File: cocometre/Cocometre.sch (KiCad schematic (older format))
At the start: 20 parts, among them P1 CONN_01X05, P2 CONN_01X05, U2 LTC4316

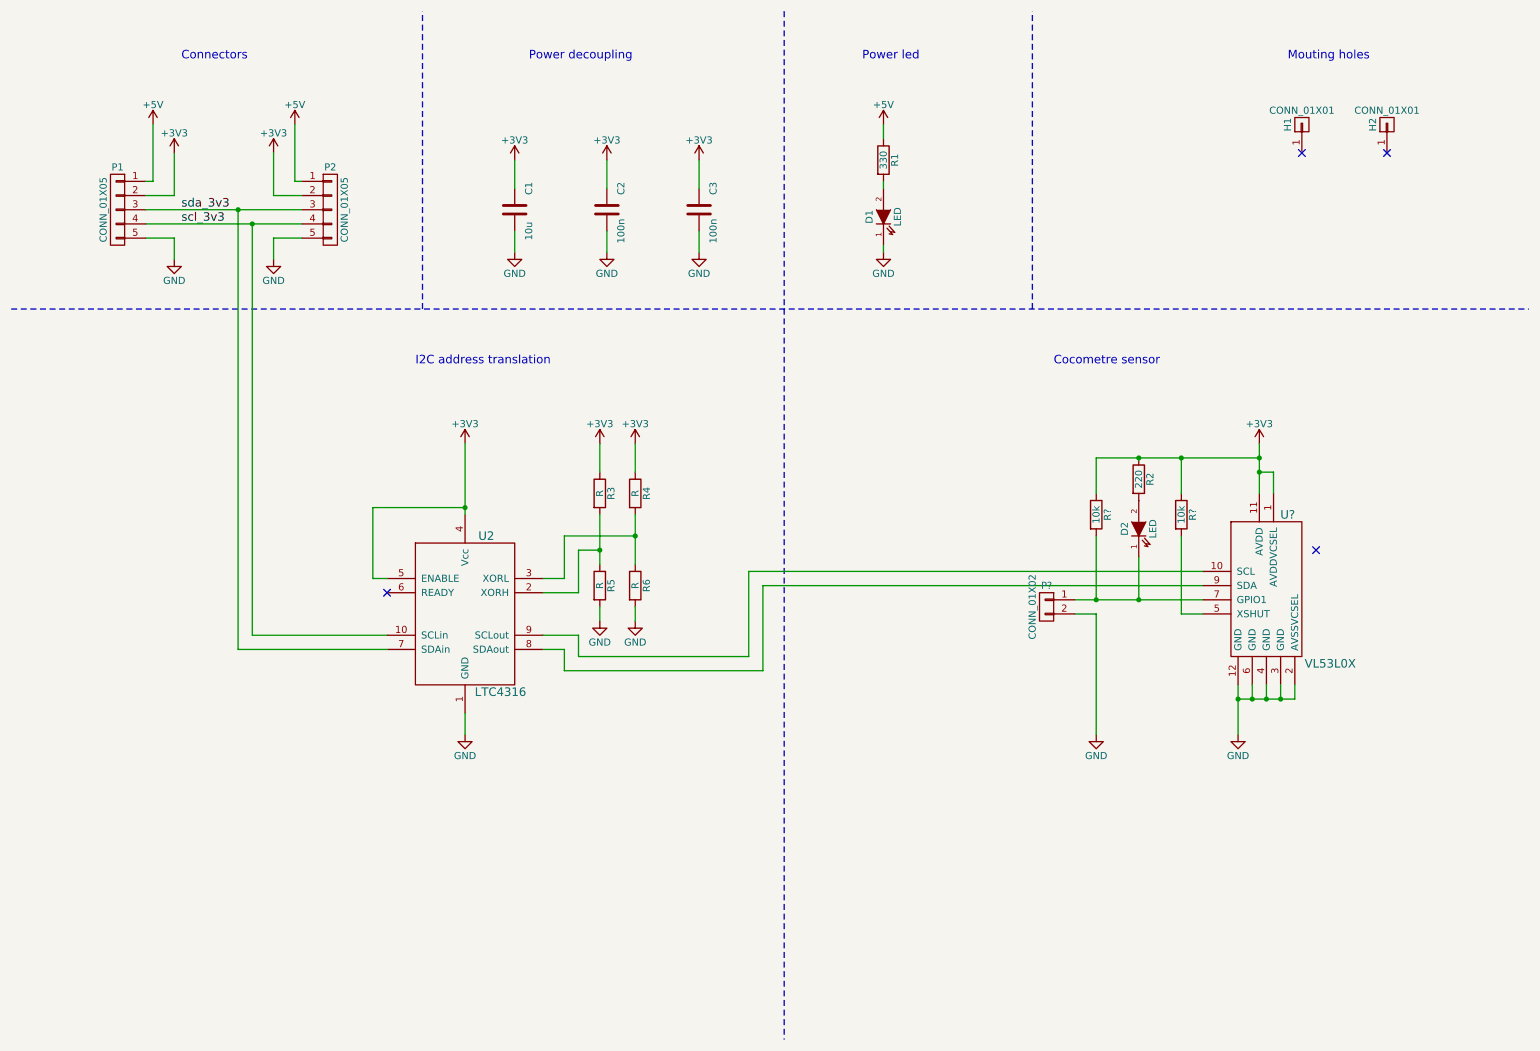
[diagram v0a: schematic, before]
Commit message: Cocometre layout
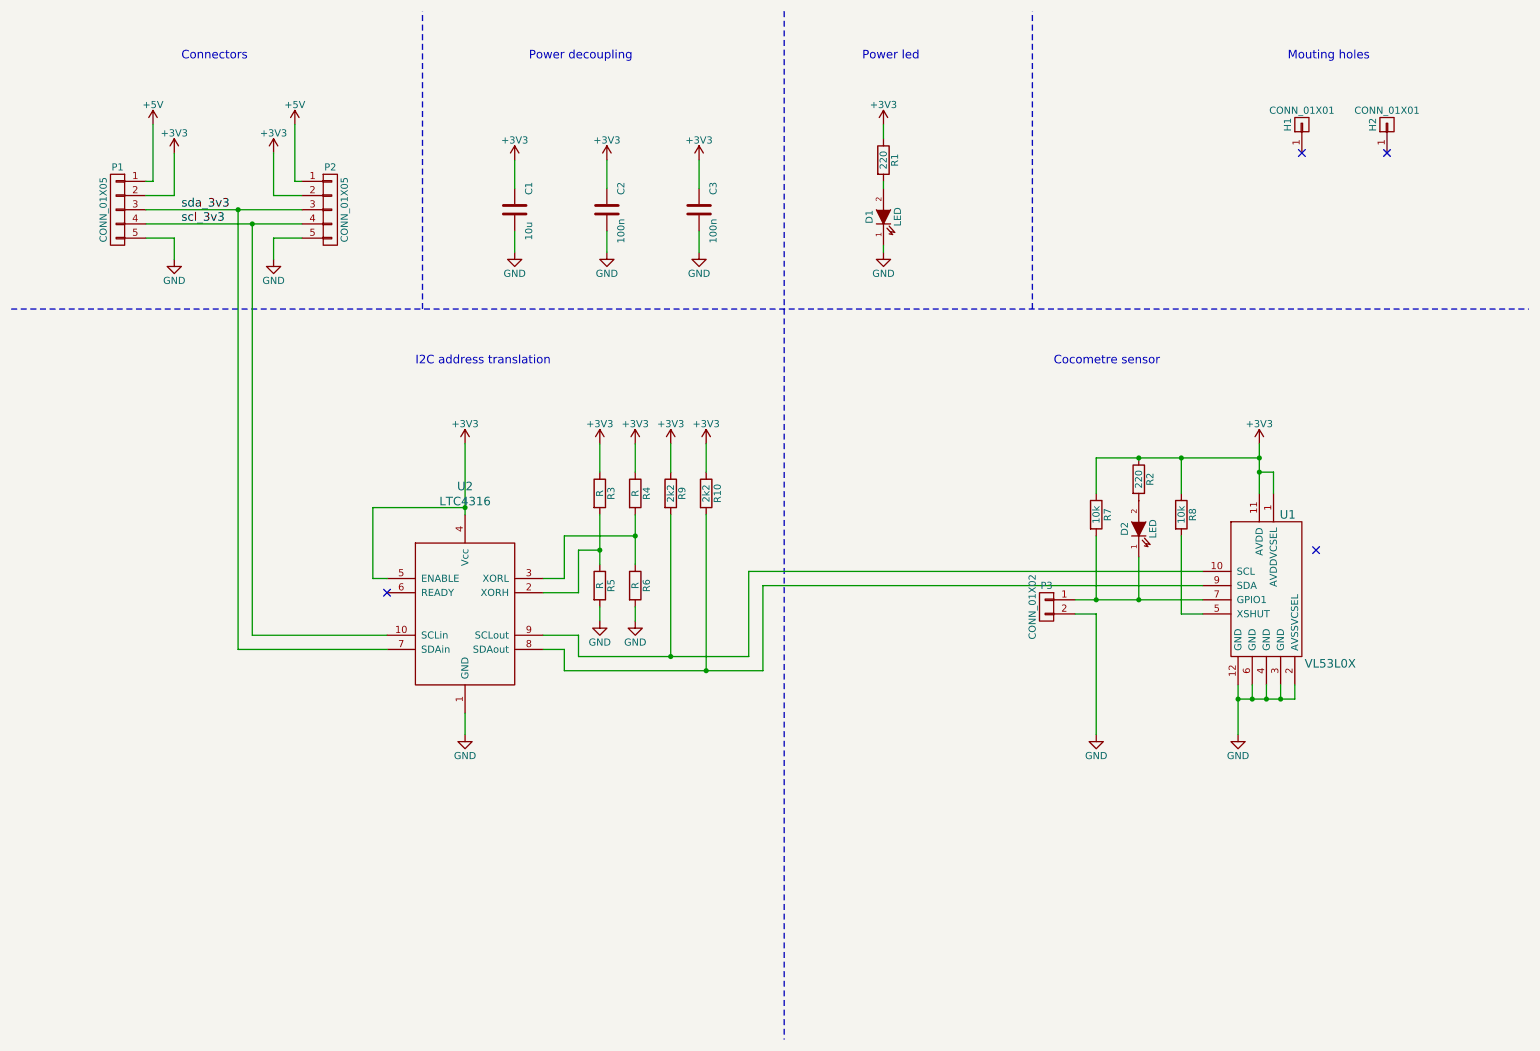
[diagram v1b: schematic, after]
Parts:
- added R10, R9: 2k2, espitall:R_0603_HandSoldering, symbol R
- C1: footprint (none) -> espitall:C_0805_HandSoldering
- C2, C3: footprint (none) -> espitall:C_0603_HandSoldering
- D1, D2: footprint (none) -> espitall:LED_0805
- H1, H2: footprint (none) -> Mounting_Holes:MountingHole_3.2mm_M3
- P1, P2: footprint (none) -> espitall:Socket_MOLEX-KK-RM2-54mm_Lock_5pin_straight
- P3: renamed from P?; footprint (none) -> espitall:Socket_MOLEX-KK-RM2-54mm_Lock_2pin_straight
- R1: value 330 -> 220; footprint (none) -> espitall:R_0603_HandSoldering
- R2, R3, R4, R5, R6: footprint (none) -> espitall:R_0603_HandSoldering
- R7, R8: renamed from R?; footprint (none) -> espitall:R_0603_HandSoldering
- U1: renamed from U?; footprint (none) -> espitall:VL53L0X
- U2: footprint (none) -> espitall:MSOP-10
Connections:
- net +3V3: now also R1.1, R10.1, R9.1
- net +5V: no longer R1.1
- net at U1.9 (SDA), U2.8 (SDAout): now also R10.2
- net at U1.10 (SCL), U2.9 (SCLout): now also R9.2
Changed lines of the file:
@@
-EESchema Schematic File Version 2
-LIBS:xilinx
-LIBS:video
-LIBS:valves
-LIBS:ttl_ieee
-LIBS:transistors
-LIBS:transf
-LIBS:texas
-LIBS:switches
-LIBS:supertex
-LIBS:stm8
-LIBS:stm32
-LIBS:siliconi
-LIBS:silabs
-LIBS:sensors
-LIBS:rfcom
-LIBS:relays
-LIBS:regul
-LIBS:references
-LIBS:powerint
-LIBS:power
-LIBS:philips
-LIBS:opto
-LIBS:onsemi
-LIBS:nxp_armmcu
-LIBS:nordicsemi
-LIBS:msp430
-LIBS:motorola
-LIBS:motor_drivers
-LIBS:microcontrollers
-LIBS:microchip_pic32mcu
-LIBS:microchip_pic18mcu
-LIBS:microchip_pic16mcu
-LIBS:microchip_pic12mcu
-LIBS:microchip_pic10mcu
-LIBS:microchip_dspic33dsc
-LIBS:microchip
-LIBS:memory
-LIBS:maxim
-LIBS:logo
-LIBS:linear
-LIBS:ir
-LIBS:interface
-LIBS:intel
-LIBS:hc11
-LIBS:graphic
-LIBS:gennum
-LIBS:ftdi
-LIBS:elec-unifil
-LIBS:dsp
-LIBS:display
-LIBS:diode
-LIBS:digital-audio
-LIBS:device
-LIBS:dc-dc
-LIBS:cypress
-LIBS:contrib
-LIBS:conn
-LIBS:cmos_ieee
-LIBS:cmos4000
-LIBS:brooktre
-LIBS:audio
-LIBS:atmel
-LIBS:analog_switches
-LIBS:analog_devices
-LIBS:adc-dac
-LIBS:actel
-LIBS:ac-dc
-LIBS:Zilog
-LIBS:Xicor
-LIBS:Power_Management
-LIBS:Oscillators
-LIBS:Lattice
-LIBS:ESD_Protection
-LIBS:Altera
-LIBS:74xx
-LIBS:74xgxx
-LIBS:Symbols_Transformer-Diskrete_RevA
-LIBS:Symbols_Socket-DIN41612_RevA
-LIBS:Symbols_Microcontroller_Philips-NXP_RevA_06Oct2013
-LIBS:Symbols_ICs-Opto_RevB_16Sep2013
-LIBS:Symbols_ICs-Diskrete_RevD10
-LIBS:Symbols_EN60617_13Mar2013
-LIBS:Symbols_EN60617-10_HF-Radio_DRAFT_12Sep2013
-LIBS:Symbols_DCDC-ACDC-Converter_RevC_20Jul2012
-LIBS:SymbolsSimilarEN60617+oldDIN617-RevE8
+EESchema Schematic File Version 3
 LIBS:espitall
 LIBS:Cocometre-cache
-EELAYER 25 0
+EELAYER 26 0
 EELAYER END
 $Descr A4 11693 8268
@@
 $EndComp
 $Comp
-L LTC4316 U2
-U 1 1 573CCB68
-P 3700 4750
-F 0 "U2" H 3850 5300 60  0000 C CNN
-F 1 "LTC4316" H 3950 4200 60  0000 C CNN
-F 2 "" H 3700 4750 60  0000 C CNN
-F 3 "" H 3700 4750 60  0000 C CNN
-	1    3700 4750
-	1    0    0    -1
-$EndComp
-$Comp
 L R R3
 U 1 1 573CCC48
@@
 F 0 "R3" V 4730 3900 50  0000 C CNN
 F 1 "R" V 4650 3900 50  0000 C CNN
-F 2 "" H 4650 3900 50  0000 C CNN
+F 2 "espitall:R_0603_HandSoldering" H 4650 3900 50  0001 C CNN
 F 3 "" H 4650 3900 50  0000 C CNN
 	1    4650 3900
@@
 F 0 "R5" V 4730 4550 50  0000 C CNN
 F 1 "R" V 4650 4550 50  0000 C CNN
-F 2 "" H 4650 4550 50  0000 C CNN
+F 2 "espitall:R_0603_HandSoldering" H 4650 4550 50  0001 C CNN
 F 3 "" H 4650 4550 50  0000 C CNN
 	1    4650 4550
@@
 F 0 "R6" V 4980 4550 50  0000 C CNN
 F 1 "R" V 4900 4550 50  0000 C CNN
-F 2 "" H 4900 4550 50  0000 C CNN
+F 2 "espitall:R_0603_HandSoldering" H 4900 4550 50  0001 C CNN
 F 3 "" H 4900 4550 50  0000 C CNN
 	1    4900 4550
@@
 F 0 "R4" V 4980 3900 50  0000 C CNN
 F 1 "R" V 4900 3900 50  0000 C CNN
-F 2 "" H 4900 3900 50  0000 C CNN
+F 2 "espitall:R_0603_HandSoldering" H 4900 3900 50  0001 C CNN
 F 3 "" H 4900 3900 50  0000 C CNN
 	1    4900 3900
@@
 F 0 "P2" H 2750 2200 50  0000 C CNN
 F 1 "CONN_01X05" V 2850 1900 50  0000 C CNN
-F 2 "" H 2750 1900 50  0000 C CNN
+F 2 "espitall:Socket_MOLEX-KK-RM2-54mm_Lock_5pin_straight" H 2750 1900 50  0001 C CNN
 F 3 "" H 2750 1900 50  0000 C CNN
 	1    2750 1900
@@
 F 0 "D2" H 8450 4250 50  0000 C CNN
 F 1 "LED" H 8450 4050 50  0000 C CNN
-F 2 "" H 8450 4150 50  0000 C CNN
+F 2 "espitall:LED_0805" H 8450 4150 50  0001 C CNN
 F 3 "" H 8450 4150 50  0000 C CNN
 	1    8450 4150
@@
 F 0 "R2" V 8530 3800 50  0000 C CNN
 F 1 "220" V 8450 3800 50  0000 C CNN
-F 2 "" H 8450 3800 50  0000 C CNN
+F 2 "espitall:R_0603_HandSoldering" H 8450 3800 50  0001 C CNN
 F 3 "" H 8450 3800 50  0000 C CNN
 	1    8450 3800
@@
 F 0 "D1" H 6650 2050 50  0000 C CNN
 F 1 "LED" H 6650 1850 50  0000 C CNN
-F 2 "" H 6650 1950 50  0000 C CNN
+F 2 "espitall:LED_0805" H 6650 1950 50  0001 C CNN
 F 3 "" H 6650 1950 50  0000 C CNN
 	1    6650 1950
@@
 $EndComp
 $Comp
-L +5V #PWR024
-U 1 1 573CEA9A
-P 6650 1300
-F 0 "#PWR024" H 6650 1150 50  0001 C CNN
-F 1 "+5V" H 6650 1440 50  0000 C CNN
-F 2 "" H 6650 1300 50  0000 C CNN
-F 3 "" H 6650 1300 50  0000 C CNN
-	1    6650 1300
-	1    0    0    -1
-$EndComp
-$Comp
 L R R1
 U 1 1 573CEAA0
 P 6650 1550
 F 0 "R1" V 6730 1550 50  0000 C CNN
-F 1 "330" V 6650 1550 50  0000 C CNN
-F 2 "" H 6650 1550 50  0000 C CNN
+F 1 "220" V 6650 1550 50  0000 C CNN
+F 2 "espitall:R_0603_HandSoldering" H 6650 1550 50  0001 C CNN
 F 3 "" H 6650 1550 50  0000 C CNN
 	1    6650 1550
@@
 F 0 "H1" H 9600 1400 50  0000 C CNN
 F 1 "CONN_01X01" V 9700 1300 50  0000 C CNN
-F 2 "" H 9600 1300 50  0000 C CNN
+F 2 "Mounting_Holes:MountingHole_3.2mm_M3" H 9600 1300 50  0001 C CNN
 F 3 "" H 9600 1300 50  0000 C CNN
 	1    9600 1300
@@
 F 0 "H2" H 10200 1400 50  0000 C CNN
 F 1 "CONN_01X01" V 10300 1300 50  0000 C CNN
-F 2 "" H 10200 1300 50  0000 C CNN
+F 2 "Mounting_Holes:MountingHole_3.2mm_M3" H 10200 1300 50  0001 C CNN
 F 3 "" H 10200 1300 50  0000 C CNN
 	1    10200 1300
@@
 F 0 "C3" V 5450 2050 50  0000 C CNN
 F 1 "100n" V 5450 1750 50  0000 C CNN
-F 2 "" H 5350 1900 50  0000 C CNN
+F 2 "espitall:C_0603_HandSoldering" H 5350 1900 50  0001 C CNN
 F 3 "" H 5350 1900 50  0000 C CNN
 	1    5350 1900
@@
 F 0 "C2" V 4800 2050 50  0000 C CNN
 F 1 "100n" V 4800 1750 50  0000 C CNN
-F 2 "" H 4700 1900 50  0000 C CNN
+F 2 "espitall:C_0603_HandSoldering" H 4700 1900 50  0001 C CNN
 F 3 "" H 4700 1900 50  0000 C CNN
 	1    4700 1900
@@
 F 0 "C1" V 4150 2050 50  0000 C CNN
 F 1 "10u" V 4150 1750 50  0000 C CNN
-F 2 "" H 4050 1900 50  0000 C CNN
+F 2 "espitall:C_0805_HandSoldering" H 4050 1900 50  0001 C CNN
 F 3 "" H 4050 1900 50  0000 C CNN
 	1    4050 1900
@@
 $EndComp
 $Comp
-L VL53L0X U?
+L VL53L0X U1
 U 1 1 57875F17
 P 9350 4750
-F 0 "U?" H 9500 5450 60  0000 C CNN
+F 0 "U1" H 9500 5450 60  0000 C CNN
 F 1 "VL53L0X" H 9800 4400 60  0000 C CNN
-F 2 "" H 9350 4750 60  0000 C CNN
+F 2 "espitall:VL53L0X" H 9350 4750 60  0001 C CNN
 F 3 "" H 9350 4750 60  0000 C CNN
 	1    9350 4750
@@
 $EndComp
 $Comp
-L GND #PWR?
+L GND #PWR018
 U 1 1 57876272
 P 9150 5600
-F 0 "#PWR?" H 9150 5350 50  0001 C CNN
+F 0 "#PWR018" H 9150 5350 50  0001 C CNN
 F 1 "GND" H 9150 5450 50  0000 C CNN
 F 2 "" H 9150 5600 50  0000 C CNN
@@
 $EndComp
 $Comp
-L R R?
+L R R8
 U 1 1 57876B49
 P 8750 4050
-F 0 "R?" V 8830 4050 50  0000 C CNN
+F 0 "R8" V 8830 4050 50  0000 C CNN
 F 1 "10k" V 8750 4050 50  0000 C CNN
-F 2 "" H 8750 4050 50  0000 C CNN
+F 2 "espitall:R_0603_HandSoldering" H 8750 4050 50  0001 C CNN
 F 3 "" H 8750 4050 50  0000 C CNN
 	1    8750 4050
@@
 F 0 "P1" H 1250 2200 50  0000 C CNN
 F 1 "CONN_01X05" V 1350 1900 50  0000 C CNN
-F 2 "" H 1250 1900 50  0000 C CNN
+F 2 "espitall:Socket_MOLEX-KK-RM2-54mm_Lock_5pin_straight" H 1250 1900 50  0001 C CNN
 F 3 "" H 1250 1900 50  0000 C CNN
 	1    1250 1900
@@
 $EndComp
 $Comp
-L CONN_01X02 P?
+L CONN_01X02 P3
 U 1 1 578781E5
 P 7800 4700
-F 0 "P?" H 7800 4850 50  0000 C CNN
+F 0 "P3" H 7800 4850 50  0000 C CNN
 F 1 "CONN_01X02" V 7900 4700 50  0000 C CNN
-F 2 "" H 7800 4700 50  0000 C CNN
+F 2 "espitall:Socket_MOLEX-KK-RM2-54mm_Lock_2pin_straight" H 7800 4700 50  0001 C CNN
 F 3 "" H 7800 4700 50  0000 C CNN
 	1    7800 4700
@@
 $EndComp
 $Comp
-L GND #PWR?
+L GND #PWR021
 U 1 1 5787831F
 P 8150 5600
-F 0 "#PWR?" H 8150 5350 50  0001 C CNN
+F 0 "#PWR021" H 8150 5350 50  0001 C CNN
 F 1 "GND" H 8150 5450 50  0000 C CNN
 F 2 "" H 8150 5600 50  0000 C CNN
@@
 	8150 4750 8000 4750
 $Comp
-L R R?
+L R R7
 U 1 1 57878471
 P 8150 4050
-F 0 "R?" V 8230 4050 50  0000 C CNN
+F 0 "R7" V 8230 4050 50  0000 C CNN
 F 1 "10k" V 8150 4050 50  0000 C CNN
-F 2 "" H 8150 4050 50  0000 C CNN
+F 2 "espitall:R_0603_HandSoldering" H 8150 4050 50  0001 C CNN
 F 3 "" H 8150 4050 50  0000 C CNN
 	1    8150 4050
@@
 Connection ~ 8150 4650
 Connection ~ 8450 4650
+$Comp
+L LTC4316 U2
+U 1 1 59ECB7A7
+P 3700 4750
+F 0 "U2" H 3700 5650 60  0000 C CNN
+F 1 "LTC4316" H 3700 5544 60  0000 C CNN
+F 2 "espitall:MSOP-10" H 3750 5200 60  0001 C CNN
+F 3 "" H 3700 4750 60  0000 C CNN
+	1    3700 4750
+	1    0    0    -1
+$EndComp
+$Comp
+L R R9
+U 1 1 59ECC069
+P 5150 3900
+F 0 "R9" V 5230 3900 50  0000 C CNN
+F 1 "2k2" V 5150 3900 50  0000 C CNN
+F 2 "espitall:R_0603_HandSoldering" H 5150 3900 50  0001 C CNN
+F 3 "" H 5150 3900 50  0000 C CNN
+	1    5150 3900
+	1    0    0    -1
+$EndComp
+$Comp
+L R R10
+U 1 1 59ECC0E1
+P 5400 3900
+F 0 "R10" V 5480 3900 50  0000 C CNN
+F 1 "2k2" V 5400 3900 50  0000 C CNN
+F 2 "espitall:R_0603_HandSoldering" H 5400 3900 50  0001 C CNN
+F 3 "" H 5400 3900 50  0000 C CNN
+	1    5400 3900
+	1    0    0    -1
+$EndComp
+$Comp
+L +3V3 #PWR022
+U 1 1 59ECC2B8
+P 5150 3550
+F 0 "#PWR022" H 5150 3400 50  0001 C CNN
+F 1 "+3V3" H 5150 3690 50  0000 C CNN
+F 2 "" H 5150 3550 50  0000 C CNN
+F 3 "" H 5150 3550 50  0000 C CNN
+	1    5150 3550
+	1    0    0    -1
+$EndComp
+$Comp
+L +3V3 #PWR024
+U 1 1 59ECC2EF
+P 5400 3550
+F 0 "#PWR024" H 5400 3400 50  0001 C CNN
+F 1 "+3V3" H 5400 3690 50  0000 C CNN
+F 2 "" H 5400 3550 50  0000 C CNN
+F 3 "" H 5400 3550 50  0000 C CNN
+	1    5400 3550
+	1    0    0    -1
+$EndComp
+Wire Wire Line
+	5400 3550 5400 3750
+Wire Wire Line
+	5150 3750 5150 3550
+Wire Wire Line
+	5150 4050 5150 5050
+Connection ~ 5150 5050
+Wire Wire Line
+	5400 4050 5400 5150
+Connection ~ 5400 5150
+$Comp
+L +3V3 #PWR025
+U 1 1 59ECC721
+P 6650 1300
+F 0 "#PWR025" H 6650 1150 50  0001 C CNN
+F 1 "+3V3" H 6650 1440 50  0000 C CNN
+F 2 "" H 6650 1300 50  0000 C CNN
+F 3 "" H 6650 1300 50  0000 C CNN
+	1    6650 1300
+	1    0    0    -1
+$EndComp
 $EndSCHEMATC
